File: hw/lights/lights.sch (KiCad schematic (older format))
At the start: 20 parts, among them J1 Conn_01x19, J2 Conn_01x19, J3 Conn_01x06, J4 Conn_01x02, Q1 PSMN9R5-30YLC,115, Q2 PSMN9R5-30YLC,115, Q3 PSMN9R5-30YLC,115, Q4 PSMN9R5-30YLC,115, Q5 PSMN9R5-30YLC,115, U1 AP63205

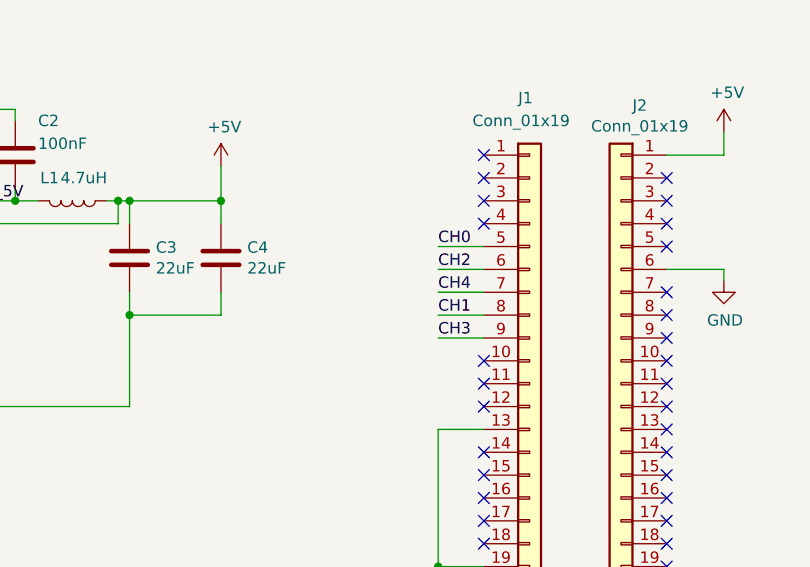
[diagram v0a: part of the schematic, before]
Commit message: sch: Add channel & IO mapping notes
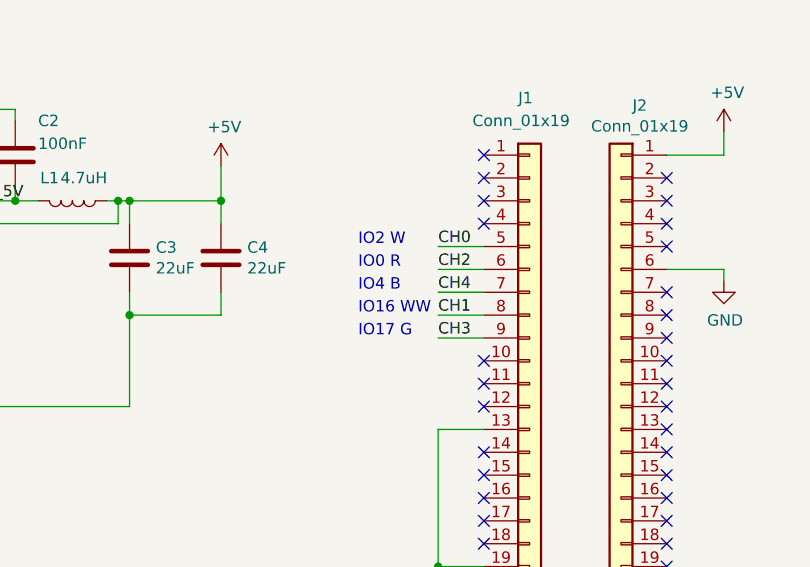
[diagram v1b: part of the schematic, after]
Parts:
- C3: footprint Capacitor_SMD:C_0805_2012Metric_Pad1.15x1.40mm_HandSolder -> Capacitor_SMD:C_0805_2012Metric_Pad1.15x1.40mm_HandSolde
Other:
- note added: "IO0 R"
- note added: "IO16 WW"
- note added: "IO17 G"
- note added: "IO2 W"
- note added: "IO4 B"
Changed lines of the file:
@@
 F 0 "C3" H 4165 3996 50  0000 L CNN
 F 1 "22uF" H 4165 3905 50  0000 L CNN
-F 2 "Capacitor_SMD:C_0805_2012Metric_Pad1.15x1.40mm_HandSolder" H 4088 3800 50  0001 C CNN
+F 2 "Capacitor_SMD:C_0805_2012Metric_Pad1.15x1.40mm_HandSolde" H 4088 3800 50  0001 C CNN
 F 3 "~" H 4050 3950 50  0001 C CNN
 	1    4050 3950
@@
 Text Notes 8150 7650 0    50   ~ 0
 2020-05-21
+Text Notes 5050 3900 0    50   ~ 0
+IO2 W
+Text Notes 5050 4000 0    50   ~ 0
+IO0 R
+Text Notes 5050 4100 0    50   ~ 0
+IO4 B
+Text Notes 5050 4200 0    50   ~ 0
+IO16 WW
+Text Notes 5050 4300 0    50   ~ 0
+IO17 G
 $EndSCHEMATC
